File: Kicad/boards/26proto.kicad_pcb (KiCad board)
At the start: 2 copper layers, 98.8 x 91.4 mm, 51 parts, among them J1 5051104096, J10 Conn_01x05, J2 Micro_SD_Card, J3 URM37, J4 RE12A, J5 RS485_TFT, J6 RS485_airdata, J7 RS485_logger_2, J8 RS485_logger, J9 BNO085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

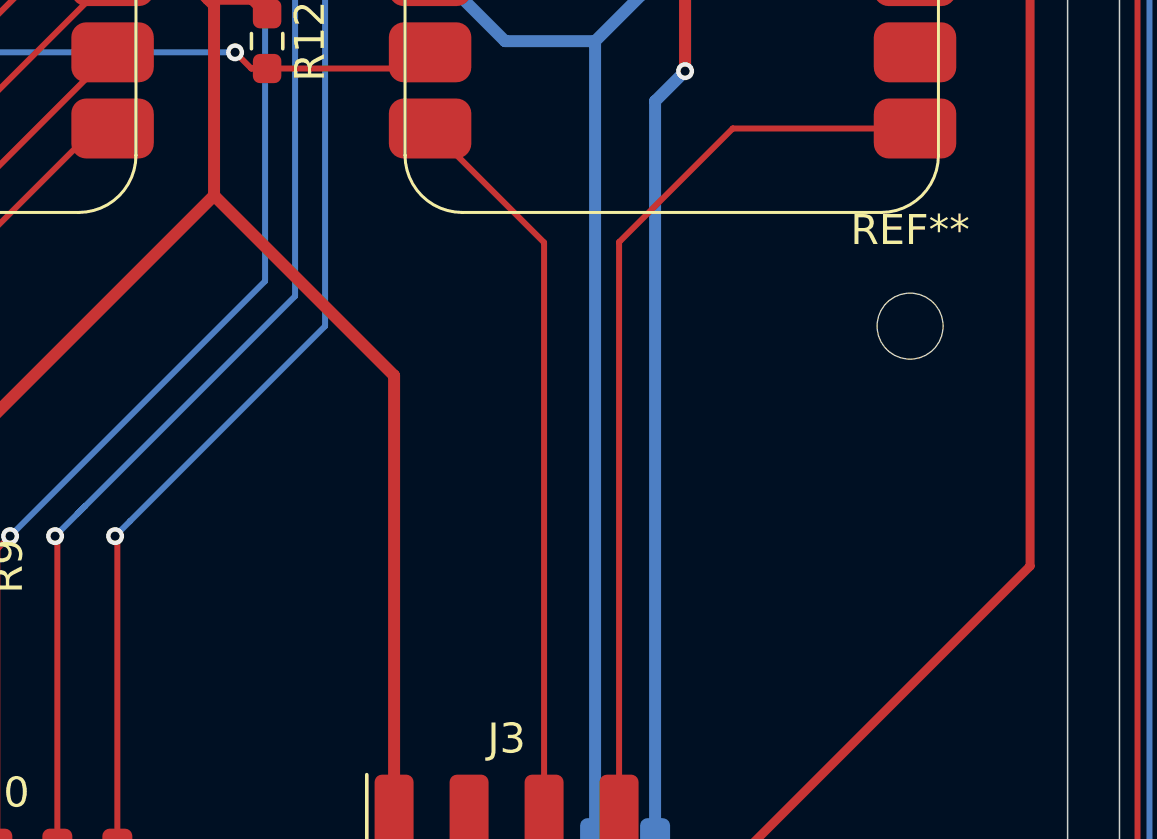
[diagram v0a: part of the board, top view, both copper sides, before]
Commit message: added mosfet
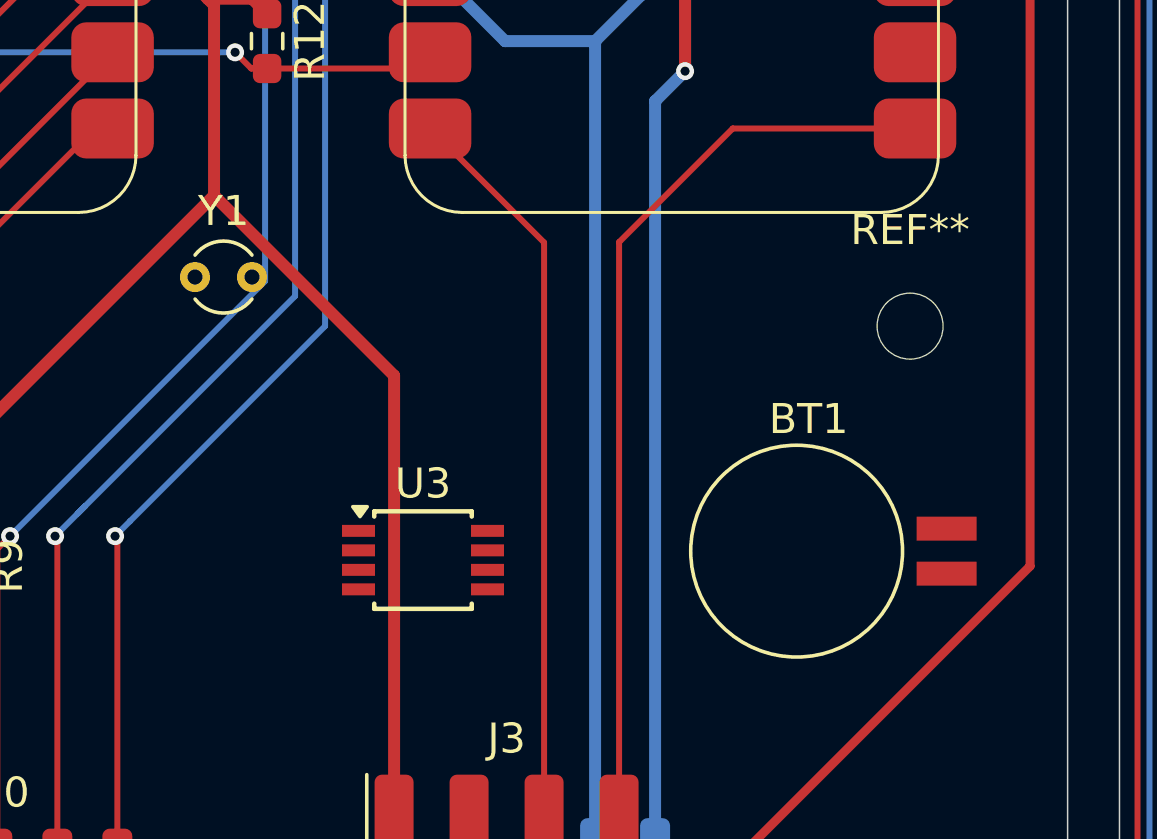
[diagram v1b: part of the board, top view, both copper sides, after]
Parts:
- added BT1: Battery_Cell, Battery:BatteryHolder_Seiko_MS621F, F.Cu at (210.7, 63.0)
- added U3: 1339D, Package_SO:TSSOP-8_3x3mm_P0.65mm, F.Cu at (193.3, 63.3)
- added Y1: CFS-206, Crystal:Crystal_DS26_D2.0mm_L6.0mm_Vertical, F.Cu at (185.7, 53.9)
- AS5601: footprint Connector_PinHeader_2.54mm:PinHeader_1x06_P2.54mm_Horizontal -> Connector_PinHeader_2.54mm:PinHeader_1x06_P2.54mm_Vertical
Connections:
- R16 pad 1: encoder_raw -> Net-(J4-Pin_2)
- R16 pad 2: Net-(J4-Pin_2) -> encoder_raw

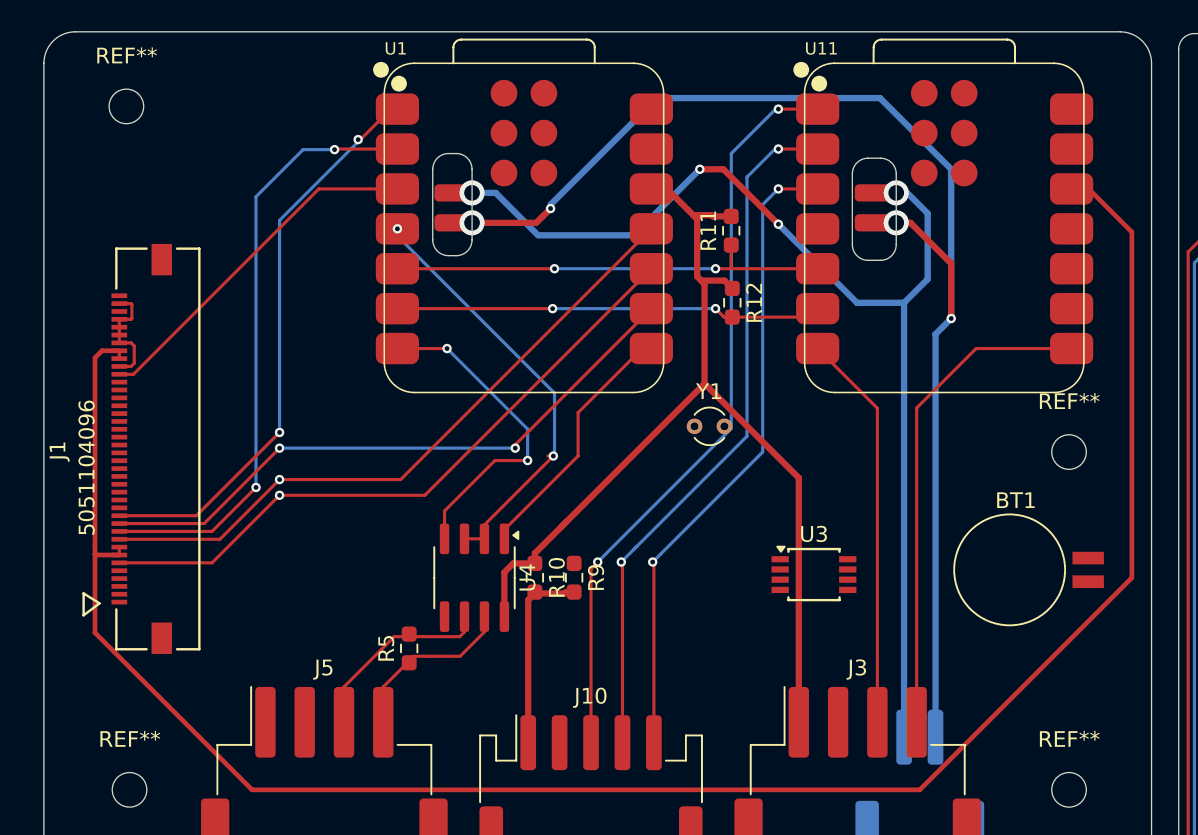
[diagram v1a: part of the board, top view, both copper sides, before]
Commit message: added RTC
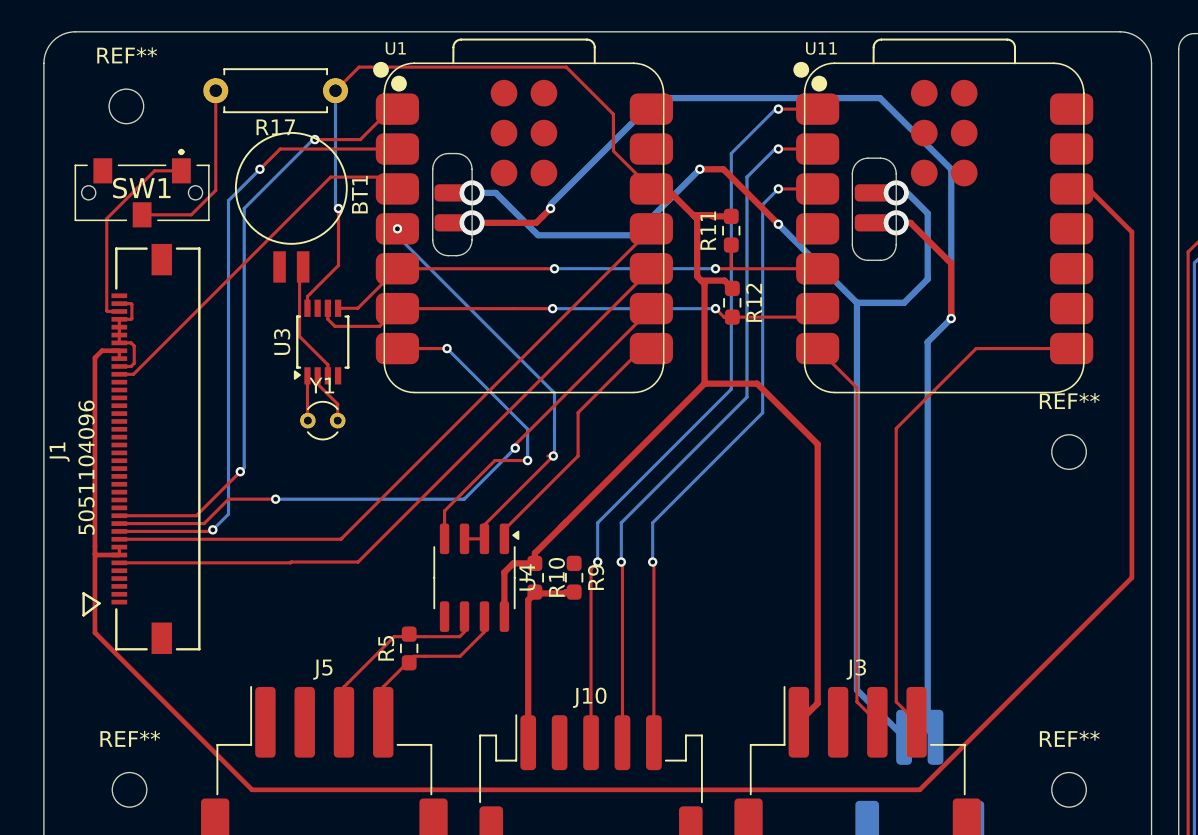
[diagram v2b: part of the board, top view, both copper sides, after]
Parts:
- added R17: R, Resistor_THT:R_Axial_DIN0207_L6.3mm_D2.5mm_P7.62mm_Horizontal, F.Cu at (162.8, 32.5)
- added SW1: SW_DIP_x01, footprints:CLSB12A02T, F.Cu at (150.5, 39.0)
- moved BT1 54.3 mm to (160.0, 43.7), turned to -90 degrees
- moved U3 34.6 mm to (162.0, 48.5), turned to 90 degrees
- moved Y1 24.6 mm to (161.1, 53.5)
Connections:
- J1 pad 34: encoder_cathode -> MOSFET_source
- J1 pad 35: encoder_cathode -> MOSFET_source
- J1 pad 36: encoder_cathode -> MOSFET_source
- J1 pad 37: encoder_cathode -> MOSFET_source
- J1 pad 38: unconnected-(J1-Pad38) -> Net-(J1-Pad38)
- U3 pad 4: (no net) -> encoder_cathode
- U3 pad 5: (no net) -> SDA_board3
- U3 pad 8: SDA_board3 -> +3.3V
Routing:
- net +3.3V: track 351.1 -> 394.1 mm, vias 4 -> 5
- net Net-(J1-Pad38): track 0.00 -> 12.7 mm
- net Net-(R17-Pad2): track 0.00 -> 11.7 mm
- net Net-(BT1-+): track 0.00 -> 7.77 mm
- net SCL_board3: track 27.2 -> 33.0 mm
- net SDA_board3: track 28.2 -> 33.0 mm
- net Net-(U3-X2): track 0.00 -> 3.38 mm
- net Net-(U3-X1): track 0.00 -> 2.86 mm
- net WRX-D/C: track 36.4 -> 38.1 mm
- net encoder_cathode: track 312.8 -> 314.0 mm
- net RX_URM37: track 31.4 -> 32.5 mm
- net CS: track 38.6 -> 39.5 mm
- net RES: track 22.6 -> 23.2 mm
- net SDO-MISO: vias 1 -> 0
- net SDA-MOSI: vias 1 -> 0

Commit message: updated
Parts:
- moved AS5600 1.18 mm to (235.8, 54.9)
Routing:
- net encoder_cathode: track 314.0 -> 317.5 mm
- net SCL_airdata: track 58.4 -> 57.2 mm
- net SDA_airdata: track 54.8 -> 53.6 mm
- net +3.3V: track 394.1 -> 392.9 mm

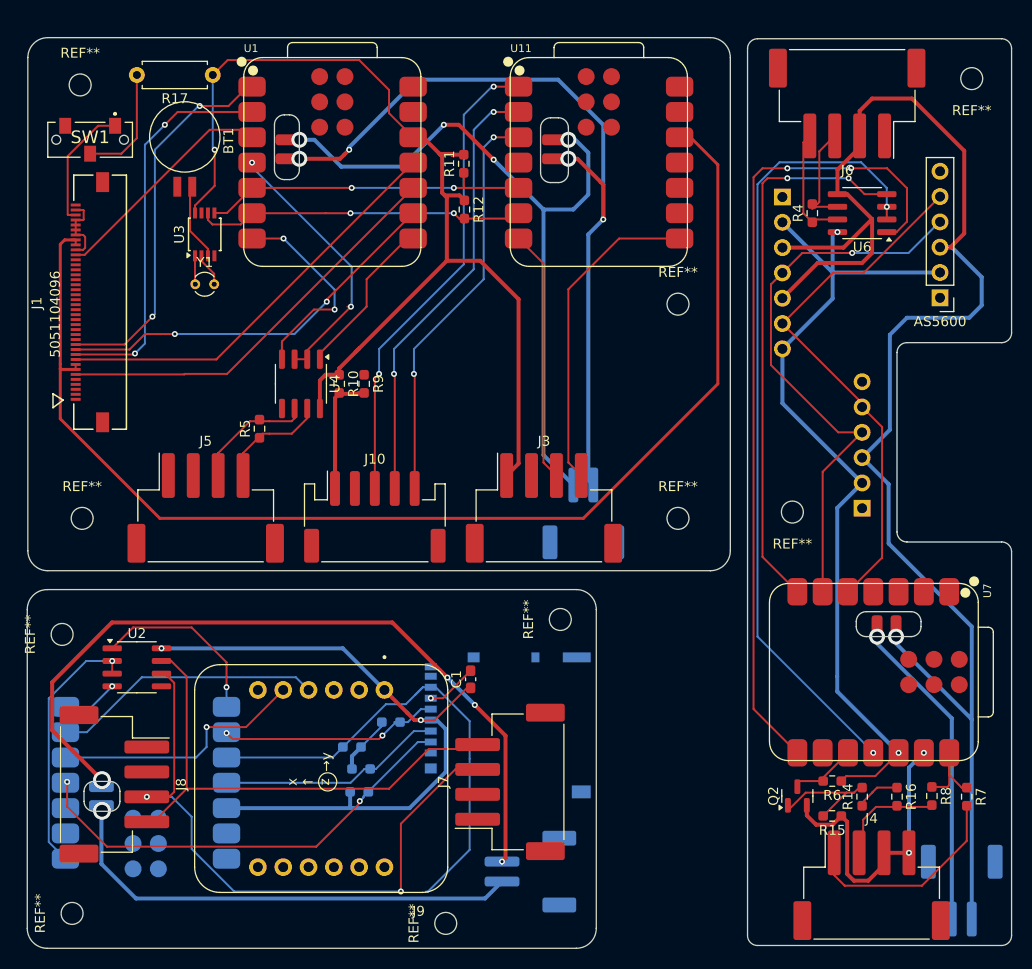
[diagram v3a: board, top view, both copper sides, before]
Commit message: add resister values
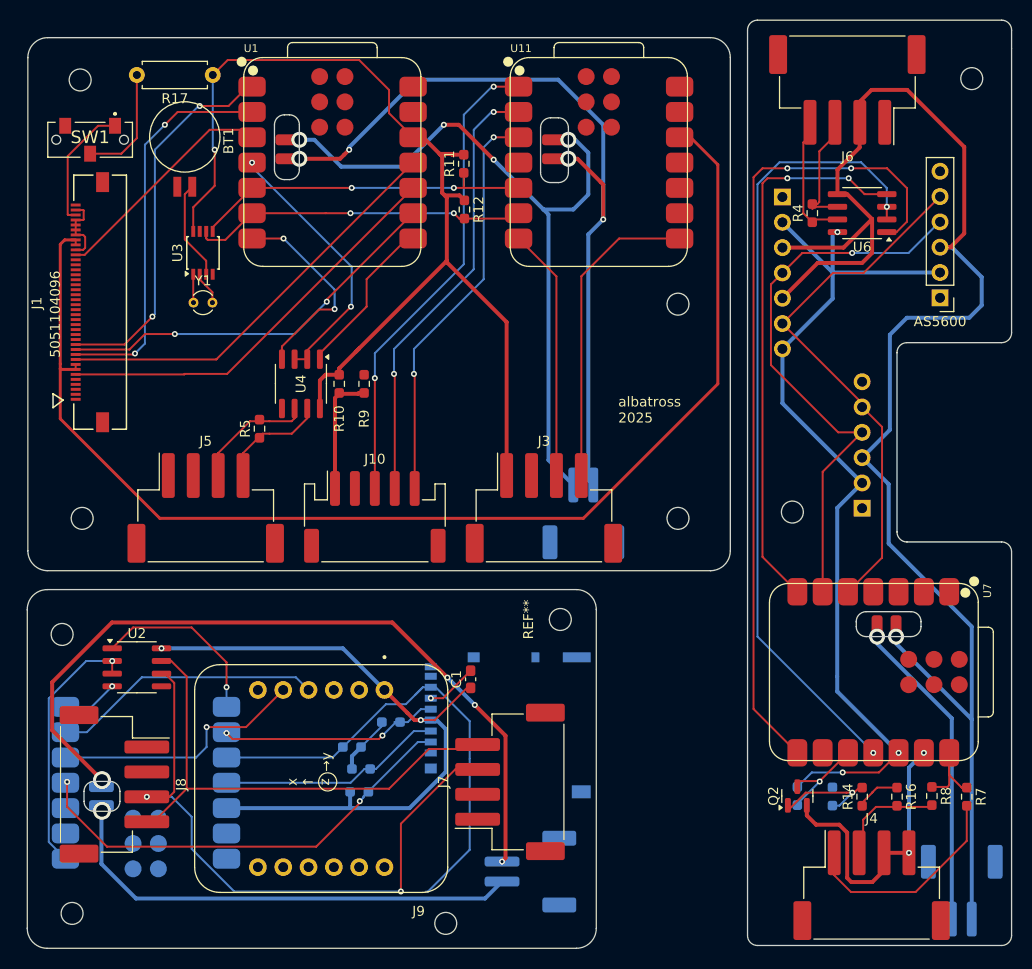
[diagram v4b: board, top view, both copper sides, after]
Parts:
- BT1: value Battery_Cell -> MS621
- C1: value C_Small -> 0.1uF
- R1, R13, R14, R16, R2, R3: value R -> 10k
- R11, R12: value R -> 3.3k
- R15: value R -> 100k; moved to B.Cu
- R17: value R -> 10
- R4, R5: value R -> 120
- R6: value R -> 10k; moved to B.Cu
- R7: value R -> 330
- R8: value R -> 3k
- moved R6 3.81 mm to (221.5, 104.9), turned to -90 degrees
- moved R15 1.95 mm to (225.0, 104.9), turned to -90 degrees
- moved U3 1.86 mm to (161.8, 50.4)
- moved Y1 1.86 mm to (160.9, 55.4)
- moved J6 1.37 mm to (226.5, 34.0)
- moved REF** 0.50 mm to (149.5, 33.0)
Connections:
- J1 pad 34: MOSFET_source -> encoder_cathode
- J1 pad 35: MOSFET_source -> encoder_cathode
- J1 pad 36: MOSFET_source -> encoder_cathode
- J1 pad 37: MOSFET_source -> encoder_cathode
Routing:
- net +3.3V: track 392.9 -> 396.5 mm, vias 5 -> 6
- net encoder_out: track 6.25 -> 9.55 mm, vias 0 -> 1
- net Net-(BT1-+): track 7.77 -> 9.98 mm
- net SDA_board3: track 33.0 -> 34.2 mm
- net RX_URM37: track 32.5 -> 31.4 mm
- net encoder_cathode: track 317.5 -> 318.3 mm
- net Net-(Q2-B): track 11.8 -> 11.0 mm, vias 0 -> 1
- net SCL_board3: track 33.0 -> 33.7 mm
- net Net-(J4-Pin_1): track 21.4 -> 21.9 mm
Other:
- board size 98.8 x 91.4 mm -> 98.8 x 93.1 mm
- board text added: "albatross 2025"

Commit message: add voltage divide resistor
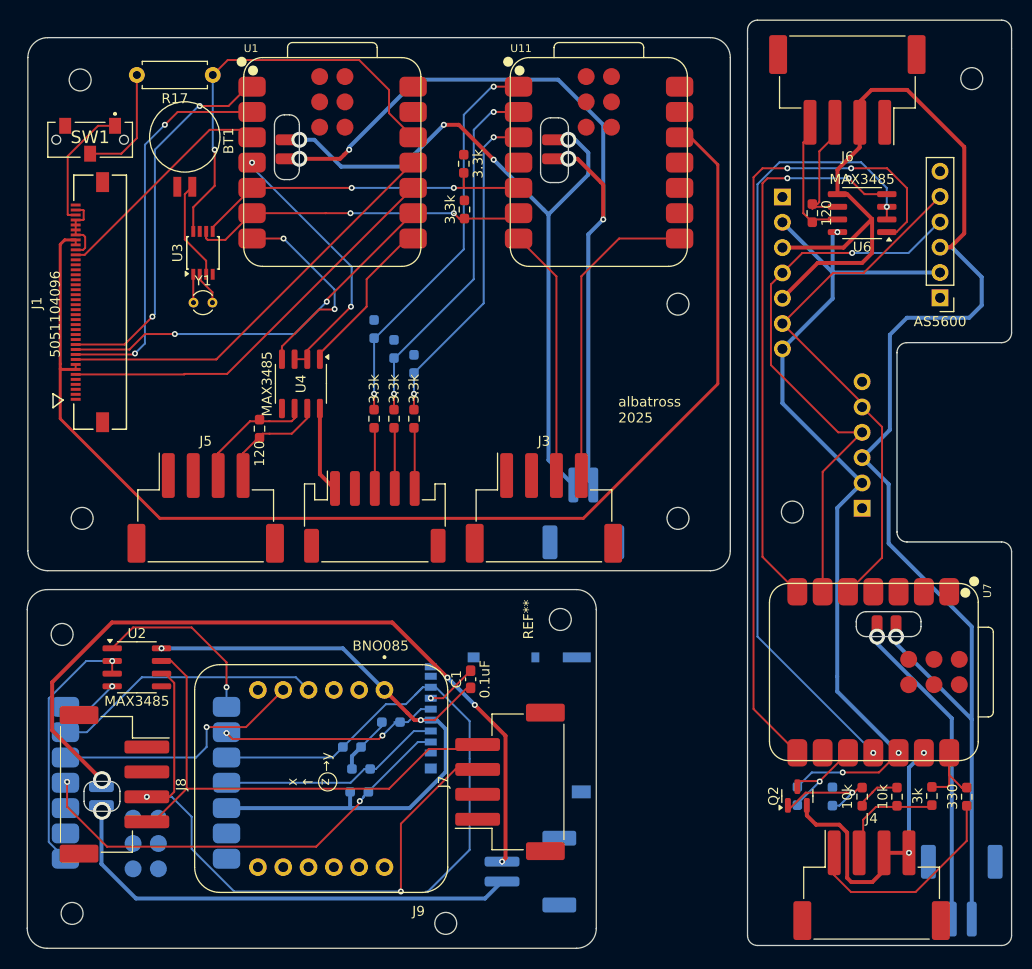
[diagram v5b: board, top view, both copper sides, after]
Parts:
- added R18: 10k, Resistor_SMD:R_0603_1608Metric_Pad0.98x0.95mm_HandSolder, B.Cu at (181.0, 60.0)
- added R19: 10k, Resistor_SMD:R_0603_1608Metric_Pad0.98x0.95mm_HandSolder, B.Cu at (183.0, 61.5)
- added R20: 3.3k, Resistor_SMD:R_0603_1608Metric_Pad0.98x0.95mm_HandSolder, F.Cu at (181.0, 67.0)
- added R21: 3.3k, Resistor_SMD:R_0603_1608Metric_Pad0.98x0.95mm_HandSolder, F.Cu at (183.0, 67.0)
- R10: value R -> 3.3k
- R9: value R -> 10k; moved to B.Cu
- moved R9 5.59 mm to (179.0, 58.0), turned to 90 degrees
- moved R10 4.95 mm to (179.0, 67.0)
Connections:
- AS5600 pad 2: +3.3V -> pot_Vin
- AS5601 pad 2: +3.3V -> pot_Vin
- C1 pad 1: +3.3V -> pot_Vin
- DPS310 pad 2: +3.3V -> pot_Vin
- DPS310 pad 7: +3.3V -> pot_Vin
- J1 pad 32: +3.3V -> pot_Vin
- J1 pad 33: +3.3V -> pot_Vin
- J1 pad 7: +3.3V -> pot_Vin
- J1 pad 8: +3.3V -> pot_Vin
- J10 pad 3: Pot_elv -> Net-(J10-Pin_3)
- J10 pad 4: Pot_rud -> Net-(J10-Pin_4)
- J10 pad 5: Pot_trim -> Net-(J10-Pin_5)
- J2 pad 4: +3.3V -> pot_Vin
- J3 pad 1: +3.3V -> pot_Vin
- J9 pad JP1_1: +3.3V -> pot_Vin
- R1 pad 2: +3.3V -> pot_Vin
- R10 pad 1: +3.3V -> Pot_elv
- R10 pad 2: pot_Vin -> Net-(J10-Pin_3)
- R11 pad 2: +3.3V -> pot_Vin
- R12 pad 1: +3.3V -> pot_Vin
- R13 pad 2: +3.3V -> pot_Vin
- R17 pad 1: +3.3V -> pot_Vin
- R2 pad 2: +3.3V -> pot_Vin
- R3 pad 2: +3.3V -> pot_Vin
- R6 pad 1: +3.3V -> pot_Vin
- R9 pad 1: encoder_cathode -> Pot_elv
- R9 pad 2: pot_Vin -> encoder_cathode
- U1 pad 12: +3.3V -> pot_Vin
- U11 pad 12: +3.3V -> pot_Vin
- U2 pad 8: +3.3V -> pot_Vin
- U3 pad 8: +3.3V -> pot_Vin
- U4 pad 8: +3.3V -> pot_Vin
- U5 pad 12: +3.3V -> pot_Vin
- U6 pad 8: +3.3V -> pot_Vin
- U7 pad 12: +3.3V -> pot_Vin
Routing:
- net +3.3V: track 396.5 -> 0.00 mm, vias 6 -> 0
- net pot_Vin: track 12.2 -> 340.5 mm, vias 0 -> 6
- net Pot_trim: track 41.1 -> 33.1 mm
- net Pot_elv: track 47.9 -> 40.0 mm
- net Pot_rud: track 44.6 -> 36.9 mm
- net Net-(J10-Pin_5): track 0.00 -> 6.12 mm
- net Net-(J10-Pin_4): track 0.00 -> 6.12 mm
- net Net-(J10-Pin_3): track 0.00 -> 6.12 mm
- net encoder_cathode: track 318.3 -> 316.8 mm

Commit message: updated pcb
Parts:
- moved R8 1.11 mm to (235.5, 105.8)
- moved R7 1.11 mm to (239.0, 105.9)
- moved R14 0.71 mm to (228.5, 105.4)
- moved R16 0.71 mm to (232.0, 105.4)
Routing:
- net MISO_SD: track 48.1 -> 23.4 mm
- net Net-(J4-Pin_2): track 10.8 -> 14.5 mm
- net encoder_raw: track 4.45 -> 3.50 mm
- net encoder_anode: track 9.58 -> 10.4 mm
- net Net-(J4-Pin_1): track 21.9 -> 21.1 mm
